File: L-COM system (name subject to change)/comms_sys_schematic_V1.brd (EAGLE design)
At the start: 43 x 72 mm, 48 parts, among them U1 TLV75733PDBVR, Y1 ECS-TXO-2016-33-120-TR

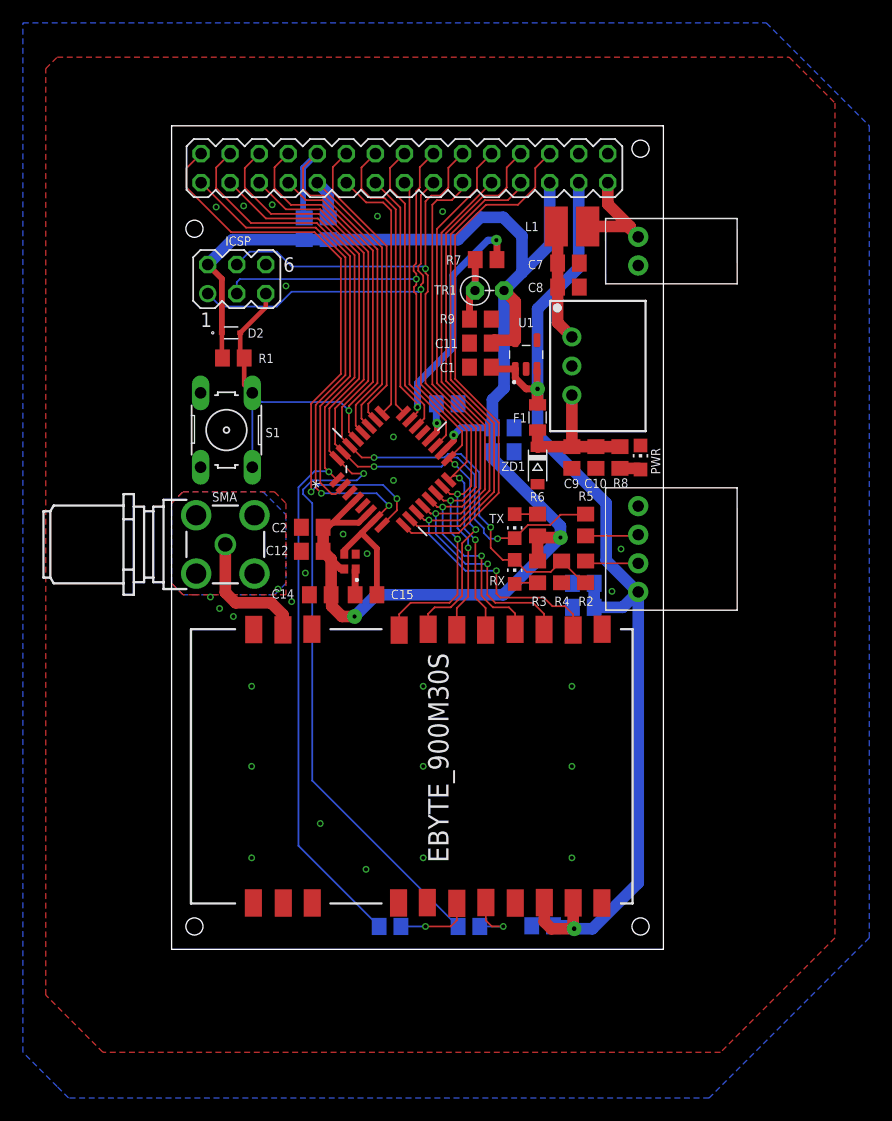
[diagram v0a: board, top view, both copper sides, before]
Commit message: Various improvements/corrections
Posted on Reddit, applied reccomendations
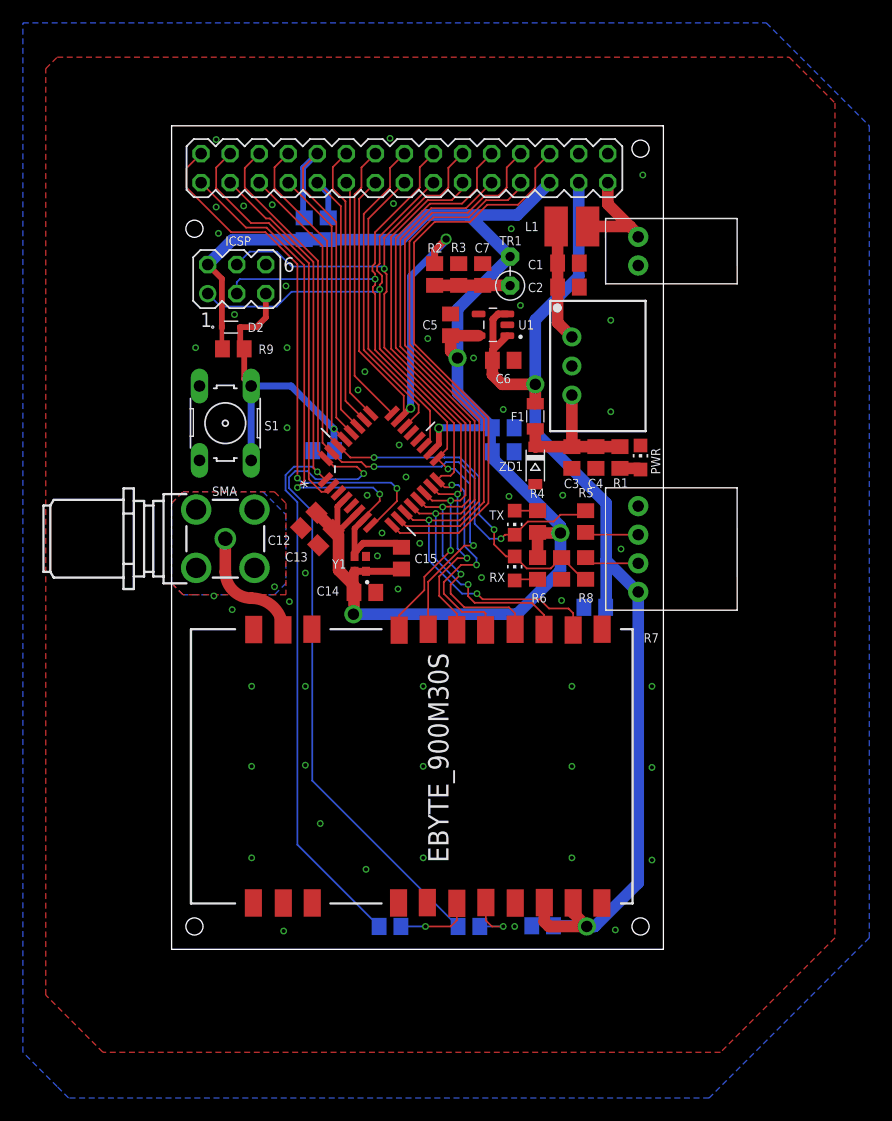
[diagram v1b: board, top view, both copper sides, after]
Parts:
- removed C9: 0.1uF, rcl:C0805
- added C17: 0.1uF, rcl:C0805
- C1, C4: value 0.1uF -> 10uF
- C10: value 10uF -> 0.01uF
- C12: value 0.01uF -> 0.1uF
- C5: value 0.1uF -> 1uF
- C6: value 10uF -> 1uF
- C7: value 10uF -> 1nF
- R1: value 10K -> 1K
- R10, R11: value 0R -> 4K7
- R12, R13: value 4K7 -> 0R
- R2: value 1K -> 0R
- R3: value 100 -> 10K
- R4: value 1K8 -> 100
- R7: value 0R -> 1K8
- moved R10 62.7 mm to (11.6, 63.0), turned to 90 degrees
- moved R13 62.7 mm to (26.0, 2.00), turned to 0 degrees
- moved R11 61.2 mm to (13.7, 63.0), turned to 90 degrees
- moved R12 61.2 mm to (19.1, 2.00), turned to 0 degrees
- moved R1 34.9 mm to (39.2, 43.0), turned to 270 degrees
- moved C2 30.7 mm to (34.7, 57.9), turned to 180 degrees
- moved R2 29.2 mm to (23.0, 59.0)
- moved C8 28.1 mm to (37.0, 29.9), flipped to the bottom
- moved R7 27.8 mm to (34.1, 33.3), turned to 90 degrees
- moved C5 27.3 mm to (24.4, 54.6), flipped to the top, turned to 270 degrees
- moved R3 26.9 mm to (25.1, 59.0), turned to 270 degrees
- moved R9 21.8 mm to (5.40, 52.5), turned to 0 degrees
- moved C6 20.7 mm to (29.0, 51.5), flipped to the top
- moved C13 18.2 mm to (13.5, 36.0), flipped to the top, turned to 45 degrees
- moved C1 11.9 mm to (34.7, 60.0), turned to 180 degrees
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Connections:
- removed net N$14: ATMEGA328P-AU.20, C3.2
- removed net N$5: C15.2, Y1.1
- removed net PC6/RESET: ATMEGA328P-AU.29, D2.A, ICSP.5, R1.2, S1.1, S1.2, SV2.7
- new net AREF: ATMEGA328P-AU.20
- new net PC6: ATMEGA328P-AU.29, C17.1, D2.A, ICSP.5, R9.2, S1.1, S1.2, SV2.7
- net $N77: now also C7.1, R2.1, R3.2; no longer R7.1, R9.2
- net +3.3V: now also C10.1, C11.1, C13.2, C15.2, C5.2, R10.1, R11.1, R4.2, R9.1, Y1.1; no longer C11.2, C13.1, C2.2, C4.1, R1.1, R12.1, R13.1, R3.2
- net +5V: now also C8.2; no longer C1.2, C5.2
- net GND: now also C10.2, C11.2, C13.1, C17.2, C4.1, C7.2, R3.1, R7.1; no longer C10.1, C11.1, C13.2, C4.2, C7.1, C9.1, R4.1, R9.1
- net N$1: now also C3.2, C4.2, R1.1; no longer C10.2, C9.2, R8.1
- net N$12: now also R6.1; no longer R3.1
- net N$16: now also R4.1; no longer R6.1
- net N$27: now also C1.2, C2.2; no longer C7.2, C8.2
- net N$4: now also R1.2; no longer R8.2
- net N$6: now also R13.1; no longer R10.1
- net N$7: now also R12.1; no longer R11.1
- net PC0: now also R2.2; no longer R7.2
- net PC4: now also R11.2; no longer R12.2
- net PC5: now also R10.2; no longer R13.2
- net PD0: now also R7.2, R8.1; no longer R2.1, R4.2
- net PD2: now also R13.2; no longer R10.2
- net PD3: now also R12.2; no longer R11.2
- net TX: now also R8.2; no longer R2.2
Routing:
- net PC6/RESET: track 53.1 -> 0.00 mm, vias 1 -> 0
- net PC6: track 0.00 -> 52.0 mm, vias 0 -> 1
- net PB1: track 53.2 -> 59.5 mm
- net PD4: track 41.3 -> 35.9 mm
- net PB6: track 55.4 -> 50.1 mm
- net PD7: track 61.6 -> 66.8 mm
- net +5V: track 97.4 -> 102.6 mm
- net PB0: track 54.0 -> 59.2 mm
- net PD6: track 41.2 -> 46.2 mm
- net PD5: track 46.4 -> 51.4 mm
- net PB4: track 63.7 -> 68.3 mm
- net PB7: track 52.1 -> 48.0 mm
- net PD0: track 62.1 -> 58.3 mm
- net PD1: track 58.8 -> 55.2 mm
- net PD3: track 79.3 -> 75.8 mm
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
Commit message: Small fixes to board. Created parts list
Still need to source resistors, capacitors, fuses, etc.

Some of the components may be sourced from elsewhere for a lot cheaper, but this list keeps it all in Digikey.
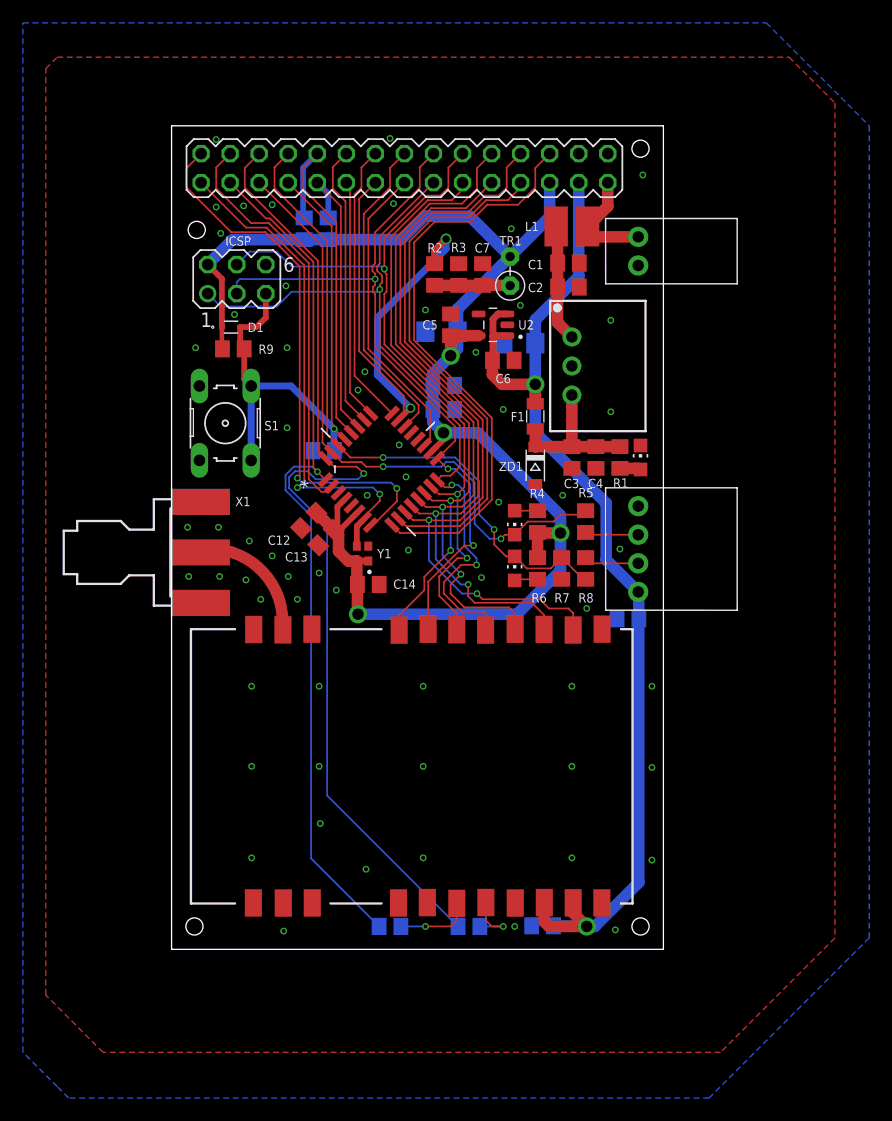
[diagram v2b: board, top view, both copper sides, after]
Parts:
- removed R-78C5.0-1.0: R-78C5.0-1.0, dc-dc-converter:SIP3
- removed SMA: BU-SMA-G, con-coax:BU-SMA-G
- added C9: 10V 22uF Tant, rcl:C1206
- added U2: TLV75733PDBVR, TLV75733PDBVR:SOT95P280X145-5N
- added X1: SMA-142-0701-801/806, con-coax:J502-ND-142-0701-801/806
- C10, C13: value 0.01uF -> 10nF
- C11, C12, C16, C17, C2, C3, C8: value 0.1uF -> 100nF
- C14: value 0.1uF -> 10nF
- C15: value 0.01uF -> 10V 22uF Tant; device rcl:C0805 -> rcl:C1206
- EBYTE: value EBYTE_SX1262_900M30S -> EBYTE_900M30S
- LED_PWR: value LED_1 -> PWR
- LED_RX: value LED_2 (Rx from ATMEGA) -> RX
- LED_TX: value LED_3 (Tx from ATMEGA) -> TX
- R4, R6: value 100 -> 100R
- U1: value TLV75733PDBVR -> R-78C5.0-1.0; device TLV75733PDBVR:SOT95P280X145-5N -> dc-dc-converter:SIP3
- moved C15 21.4 mm to (30.4, 53.0), flipped to the bottom, turned to 0 degrees
- moved U1 7.78 mm to (35.0, 51.0), turned to 270 degrees
- moved C11 6.38 mm to (23.8, 47.2)
- moved C10 6.38 mm to (23.8, 49.3)
- moved C8 3.07 mm to (39.9, 28.9)
- moved Y1 0.92 mm to (16.7, 34.6)
- moved C14 0.76 mm to (17.2, 31.9)
- renumbered ATMEGA328P-AU to MCU1, D2 to D1, EBYTE_900M30S to EBYTE, PWR to LED_PWR, RX to LED_RX, SV2 to FH1, TX to LED_TX, U$2 to MX1, U$3 to MX2
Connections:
- net +3.3V: now also C9.1, U2.5; no longer C15.2, U1.5
- net +5V: now also C15.1, U2.1, U2.3; no longer U1.1, U1.3
- net GND: now also C15.2, C9.2, U2.2, X1.G@1, X1.G@2, X1.G@3, X1.G@4; no longer R-78C5.0-1.0.2, SMA.2, SMA.3, SMA.4, SMA.5
- net N$1: now also U1.3; no longer R-78C5.0-1.0.3
- net N$27: now also U1.1; no longer R-78C5.0-1.0.1
- net N$8: now also X1.1; no longer SMA.1
- net PB6: no longer C15.1
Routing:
- net +3.3V: track 136.7 -> 129.5 mm
- net PB6: track 50.1 -> 44.5 mm
- net +5V: track 102.6 -> 97.1 mm
- net PC0: track 43.2 -> 45.6 mm
- net VIN: track 9.56 -> 10.8 mm
- net N$8: track 10.0 -> 11.0 mm
- net PB5: track 64.0 -> 64.6 mm

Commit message: V1 design finished, full parts list
First version finished, complete parts list put together.

Boards currently ordered from PCBWay to try out the design.
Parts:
- removed S1: Omron, switch-omron:B3F-10XX
- removed TR1: (no value), discrete:RS-2,5
- added R14: 0R, rcl:R0805
- added SW1: (no value), Wurth_Elektronik_Electromechanic_Switch_rev16c:430152043826
- C15, C9: value 10V 22uF Tant -> 10V 33uF Tant
- F1: value 1.5A -> 1A
- R10: value 4K7 -> 10K
- R12: value 0R -> 4K7
- R4: value 100R -> 1624345-1; device rcl:R0805 -> 1624345-1:THRMC2012X50N
- R5: value 1K -> 200R
- R6: value 100R -> 1K
- R7: value 1K8 -> 200R
- R8: value 1K -> 1K8
- R9: value 10K -> 1K
- moved R12 61.4 mm to (13.7, 63.2), turned to 90 degrees
- moved R9 36.3 mm to (36.2, 33.3), turned to 90 degrees
- moved R4 21.8 mm to (29.3, 59.0)
- moved R10 11.4 mm to (6.50, 52.8), flipped to the top, turned to 0 degrees
- moved R13 6.90 mm to (19.1, 2.00)
- moved R6 5.87 mm to (36.2, 37.4)
- moved R5 4.20 mm to (32.0, 37.4), turned to 270 degrees
- moved C17 3.69 mm to (15.7, 46.4), turned to 90 degrees
- moved R11 2.11 mm to (11.6, 63.2)
- moved R7 2.10 mm to (32.0, 33.3)
- moved R8 2.10 mm to (34.1, 33.3)
- moved D1 1.50 mm to (6.70, 54.5)
- moved FH1 0.30 mm to (22.6, 68.3)
- moved ICSP 0.10 mm to (5.60, 58.6)
- moved X1 0.10 mm to (-0.10, 34.7)
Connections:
- net $N77: now also R4.2; no longer TR1.1
- net +3.3V: now also R12.1, R4.1, R5.2, R7.2; no longer R4.2, R6.2, R9.1, TR1.2
- net GND: now also R8.1, SW1.2, SW1.4; no longer R7.1, S1.3, S1.4
- net N$12: now also R7.1; no longer R6.1
- net N$16: now also R5.1; no longer R4.1
- net N$6: now also R14.1; no longer R13.1
- net N$7: now also R13.1; no longer R12.1
- net PC4: now also R12.2; no longer R11.2
- net PC5: now also R11.2; no longer R10.2
- net PC6: now also R10.2, SW1.1, SW1.3; no longer R9.2, S1.1, S1.2
- net PD0: now also R8.2, R9.1; no longer R7.2, R8.1
- net PD1: now also R6.2; no longer R5.2
- net PD2: now also R14.2; no longer R13.2
- net PD3: now also R13.2; no longer R12.2
- net RX: now also R6.1; no longer R5.1
- net TX: now also R9.2; no longer R8.2
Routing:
- net PB7: track 48.2 -> 45.9 mm, vias 2 -> 3
- net +3.3V: track 129.5 -> 131.6 mm, vias 4 -> 5
- net PD0: track 58.0 -> 60.0 mm
- net PC6: track 52.0 -> 50.4 mm, vias 1 -> 2
- net PC0: track 45.6 -> 44.5 mm
- net +5V: track 97.1 -> 98.0 mm
- net PB5: track 64.6 -> 64.0 mm
- net PD7: track 67.0 -> 66.5 mm
- net PB2: track 51.4 -> 50.8 mm
- net PD5: track 51.6 -> 51.1 mm
- net PB1: track 59.7 -> 59.2 mm
- net PB0: track 59.4 -> 58.9 mm
- added copper zone on layer 1, net NO_GND
- added copper zone on layer 16, net NO_GND
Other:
- outline, holes or cut-outs redrawn
- board text added: "10/26/2020"
- board text added: "LCOM-V1"
